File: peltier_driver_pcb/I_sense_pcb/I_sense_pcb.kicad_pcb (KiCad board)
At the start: 2 copper layers, 59.5 x 33 mm, 34 parts, among them J1 Peltier V-, J10 Driver V-, J11 Peltier V-, J12 Driver V-, J13 Peltier V+, J14 Peltier V+, J15 Driver V+, J16 Driver V+, J17 Conn_02x10_Top_Bottom, J18 Conn_02x10_Top_Bottom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

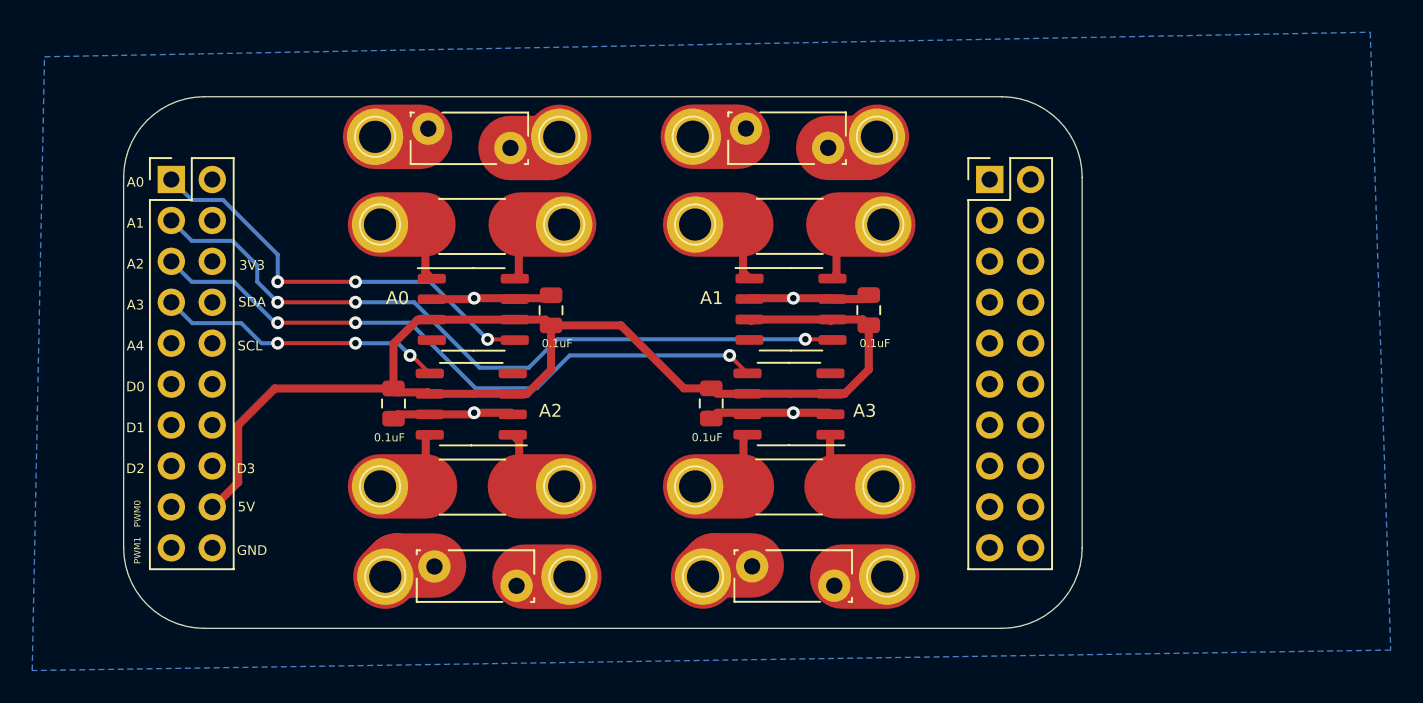
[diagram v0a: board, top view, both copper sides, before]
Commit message: matching PCB dimensions to each other
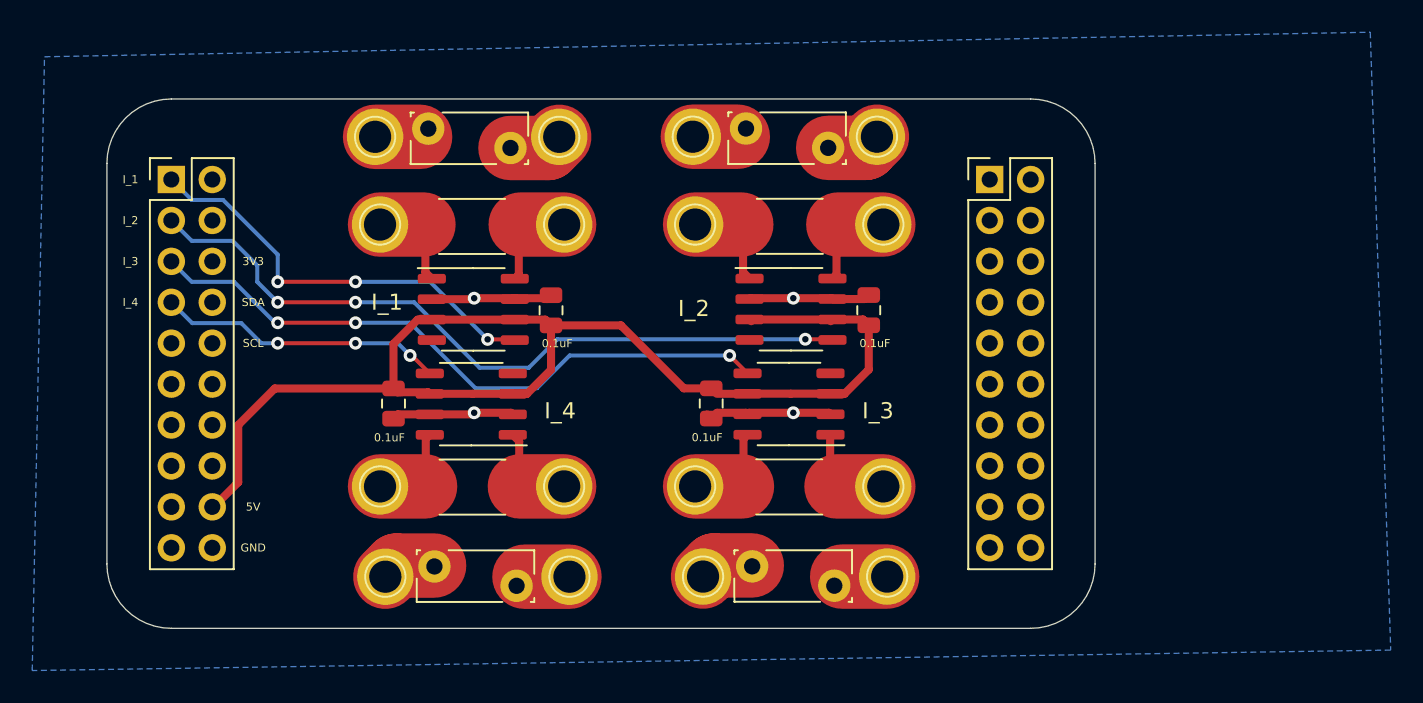
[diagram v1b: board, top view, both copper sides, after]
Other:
- board size 59.5 x 33 mm -> 61.3 x 32.9 mm
- board text added: "I_1"
- board text added: "I_2"
- board text added: "I_3"
- board text added: "I_4"
- board text removed: "A0"
- board text removed: "A1"
- board text removed: "A2"
- board text removed: "A3"
- board text removed: "A4"
- board text removed: "D0"
- board text removed: "D1"
- board text removed: "D2"
- board text removed: "D3"
- board text removed: "PWM0"
- board text removed: "PWM1"
